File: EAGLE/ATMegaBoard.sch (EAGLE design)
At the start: 29 parts, among them IC1 L298, IC2 ATMEGA168-20P, IC3 REG1117, X1 49S/18PF

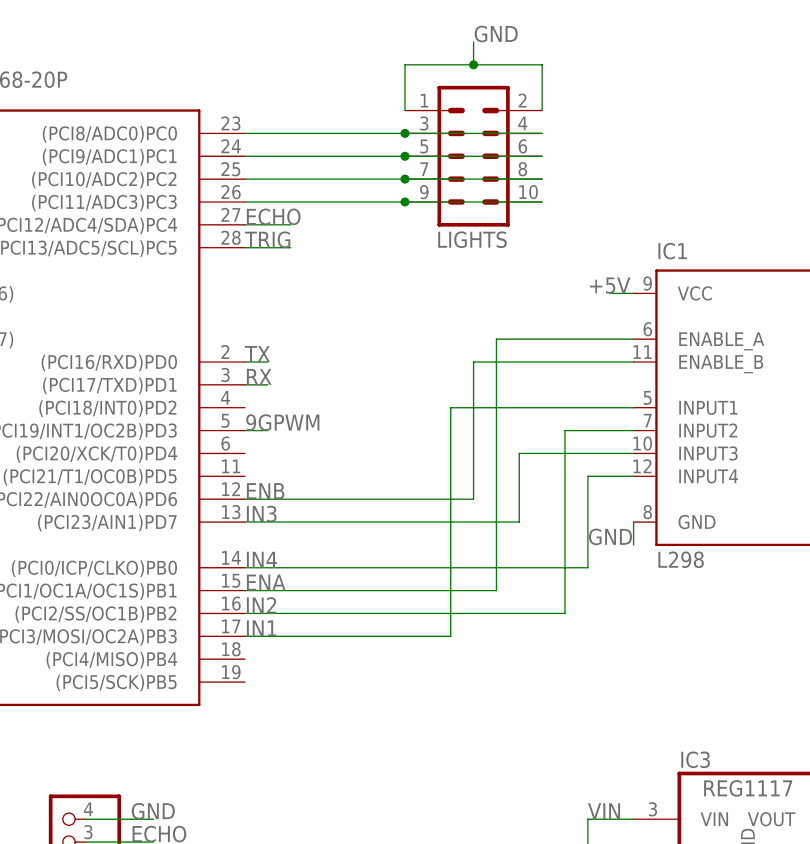
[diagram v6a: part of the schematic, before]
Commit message: updated output for LEDs
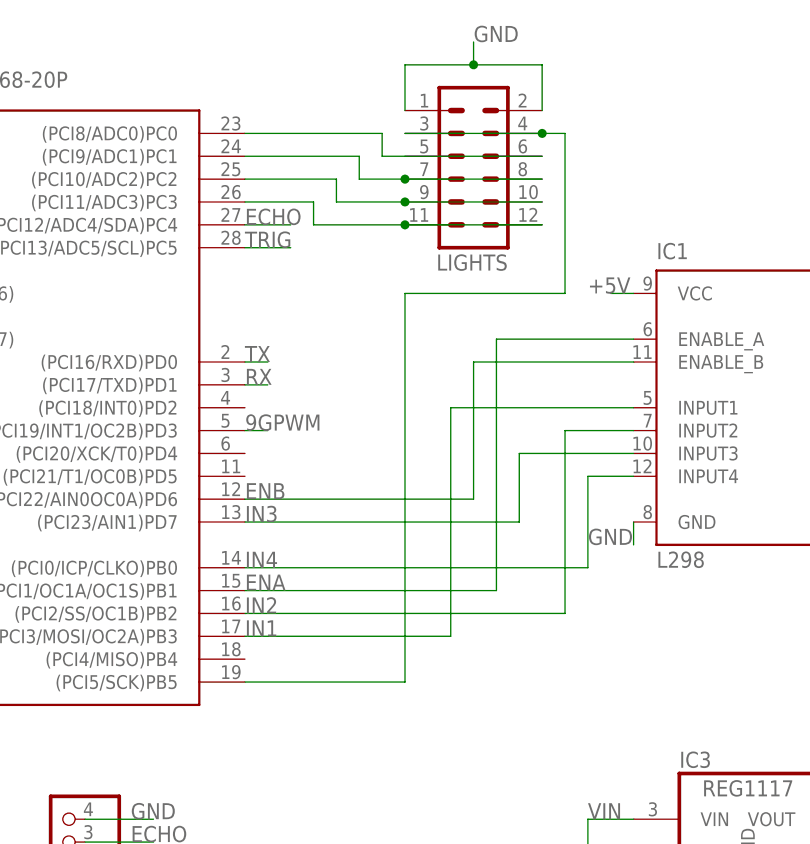
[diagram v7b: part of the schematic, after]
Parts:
- LIGHTS: device con-lstb:MA05-2 -> con-lstb:MA06-2
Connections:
- new net N$7: IC2.(PCI11/ADC3)PC3, LIGHTS.11, LIGHTS.12
- net N$1: now also IC2.(PCI5/SCK)PB5; no longer IC2.(PCI8/ADC0)PC0
- net N$2: now also IC2.(PCI8/ADC0)PC0; no longer IC2.(PCI9/ADC1)PC1
- net N$4: now also IC2.(PCI9/ADC1)PC1; no longer IC2.(PCI10/ADC2)PC2
- net N$5: now also IC2.(PCI10/ADC2)PC2; no longer IC2.(PCI11/ADC3)PC3
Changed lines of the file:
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@@
 <part name="R3" library="rcl" library_urn="urn:adsk.eagle:library:334" deviceset="R-US_" device="0207/10" package3d_urn="urn:adsk.eagle:package:23491/2" value="1k"/>
 <part name="HC05" library="con-lsta" library_urn="urn:adsk.eagle:library:161" deviceset="FE06W" device="" package3d_urn="urn:adsk.eagle:package:8198/1"/>
-<part name="LIGHTS" library="con-lstb" library_urn="urn:adsk.eagle:library:162" deviceset="MA05-2" device="" package3d_urn="urn:adsk.eagle:package:8329/1"/>
+<part name="LIGHTS" library="con-lstb" library_urn="urn:adsk.eagle:library:162" deviceset="MA06-2" device="" package3d_urn="urn:adsk.eagle:package:8342/1"/>
 </parts>
 <sheets>
@@
 <attribute name="NAME" x="110.49" y="-26.162" size="1.778" layer="95" rot="R180"/>
 </instance>
-<instance part="LIGHTS" gate="G$1" x="114.3" y="76.2" smashed="yes" rot="R180">
-<attribute name="VALUE" x="118.11" y="86.36" size="1.778" layer="96" rot="R180"/>
-<attribute name="NAME" x="118.11" y="67.818" size="1.778" layer="95" rot="R180"/>
+<instance part="LIGHTS" gate="1" x="114.3" y="73.66" smashed="yes" rot="R180">
+<attribute name="VALUE" x="118.11" y="83.82" size="1.778" layer="96" rot="R180"/>
+<attribute name="NAME" x="118.11" y="65.278" size="1.778" layer="95" rot="R180"/>
 </instance>
 </instances>
@@
 </segment>
 <segment>
-<pinref part="LIGHTS" gate="G$1" pin="1"/>
+<pinref part="LIGHTS" gate="1" pin="1"/>
 <wire x1="106.68" y1="81.28" x2="106.68" y2="86.36" width="0.1524" layer="91"/>
 <wire x1="106.68" y1="86.36" x2="114.3" y2="86.36" width="0.1524" layer="91"/>
-<pinref part="LIGHTS" gate="G$1" pin="2"/>
+<pinref part="LIGHTS" gate="1" pin="2"/>
 <wire x1="114.3" y1="86.36" x2="121.92" y2="86.36" width="0.1524" layer="91"/>
 <wire x1="121.92" y1="86.36" x2="121.92" y2="81.28" width="0.1524" layer="91"/>
@@
 <net name="N$1" class="0">
 <segment>
+<pinref part="LIGHTS" gate="1" pin="3"/>
+<pinref part="LIGHTS" gate="1" pin="4"/>
+<wire x1="106.68" y1="78.74" x2="121.92" y2="78.74" width="0.1524" layer="91"/>
+<wire x1="121.92" y1="78.74" x2="124.46" y2="78.74" width="0.1524" layer="91"/>
+<junction x="121.92" y="78.74"/>
+<wire x1="124.46" y1="78.74" x2="124.46" y2="60.96" width="0.1524" layer="91"/>
+<pinref part="IC2" gate="G$1" pin="(PCI5/SCK)PB5"/>
+<wire x1="106.68" y1="17.78" x2="88.9" y2="17.78" width="0.1524" layer="91"/>
+<wire x1="124.46" y1="60.96" x2="106.68" y2="60.96" width="0.1524" layer="91"/>
+<wire x1="106.68" y1="60.96" x2="106.68" y2="17.78" width="0.1524" layer="91"/>
+</segment>
+</net>
+<net name="N$2" class="0">
+<segment>
+<pinref part="LIGHTS" gate="1" pin="5"/>
+<pinref part="LIGHTS" gate="1" pin="6"/>
+<wire x1="106.68" y1="76.2" x2="121.92" y2="76.2" width="0.1524" layer="91"/>
 <pinref part="IC2" gate="G$1" pin="(PCI8/ADC0)PC0"/>
-<pinref part="LIGHTS" gate="G$1" pin="3"/>
-<wire x1="88.9" y1="78.74" x2="106.68" y2="78.74" width="0.1524" layer="91"/>
-<pinref part="LIGHTS" gate="G$1" pin="4"/>
-<wire x1="106.68" y1="78.74" x2="121.92" y2="78.74" width="0.1524" layer="91"/>
-<junction x="106.68" y="78.74"/>
-</segment>
-</net>
-<net name="N$2" class="0">
-<segment>
+<wire x1="88.9" y1="78.74" x2="104.14" y2="78.74" width="0.1524" layer="91"/>
+<wire x1="104.14" y1="78.74" x2="104.14" y2="76.2" width="0.1524" layer="91"/>
+<wire x1="104.14" y1="76.2" x2="106.68" y2="76.2" width="0.1524" layer="91"/>
+</segment>
+</net>
+<net name="N$4" class="0">
+<segment>
+<pinref part="LIGHTS" gate="1" pin="7"/>
+<pinref part="LIGHTS" gate="1" pin="8"/>
+<wire x1="106.68" y1="73.66" x2="121.92" y2="73.66" width="0.1524" layer="91"/>
 <pinref part="IC2" gate="G$1" pin="(PCI9/ADC1)PC1"/>
-<pinref part="LIGHTS" gate="G$1" pin="5"/>
-<wire x1="88.9" y1="76.2" x2="106.68" y2="76.2" width="0.1524" layer="91"/>
-<pinref part="LIGHTS" gate="G$1" pin="6"/>
-<wire x1="106.68" y1="76.2" x2="121.92" y2="76.2" width="0.1524" layer="91"/>
-<junction x="106.68" y="76.2"/>
-</segment>
-</net>
-<net name="N$4" class="0">
-<segment>
+<wire x1="88.9" y1="76.2" x2="101.6" y2="76.2" width="0.1524" layer="91"/>
+<wire x1="101.6" y1="76.2" x2="101.6" y2="73.66" width="0.1524" layer="91"/>
+<wire x1="101.6" y1="73.66" x2="106.68" y2="73.66" width="0.1524" layer="91"/>
+<junction x="106.68" y="73.66"/>
+</segment>
+</net>
+<net name="N$5" class="0">
+<segment>
+<pinref part="LIGHTS" gate="1" pin="9"/>
+<pinref part="LIGHTS" gate="1" pin="10"/>
+<wire x1="106.68" y1="71.12" x2="121.92" y2="71.12" width="0.1524" layer="91"/>
 <pinref part="IC2" gate="G$1" pin="(PCI10/ADC2)PC2"/>
-<pinref part="LIGHTS" gate="G$1" pin="7"/>
-<wire x1="88.9" y1="73.66" x2="106.68" y2="73.66" width="0.1524" layer="91"/>
-<pinref part="LIGHTS" gate="G$1" pin="8"/>
-<wire x1="106.68" y1="73.66" x2="121.92" y2="73.66" width="0.1524" layer="91"/>
-<junction x="106.68" y="73.66"/>
-</segment>
-</net>
-<net name="N$5" class="0">
-<segment>
+<wire x1="88.9" y1="73.66" x2="99.06" y2="73.66" width="0.1524" layer="91"/>
+<wire x1="99.06" y1="73.66" x2="99.06" y2="71.12" width="0.1524" layer="91"/>
+<wire x1="99.06" y1="71.12" x2="106.68" y2="71.12" width="0.1524" layer="91"/>
+<junction x="106.68" y="71.12"/>
+</segment>
+</net>
+<net name="N$7" class="0">
+<segment>
+<pinref part="LIGHTS" gate="1" pin="12"/>
+<pinref part="LIGHTS" gate="1" pin="11"/>
+<wire x1="106.68" y1="68.58" x2="121.92" y2="68.58" width="0.1524" layer="91"/>
 <pinref part="IC2" gate="G$1" pin="(PCI11/ADC3)PC3"/>
-<pinref part="LIGHTS" gate="G$1" pin="9"/>
-<wire x1="88.9" y1="71.12" x2="106.68" y2="71.12" width="0.1524" layer="91"/>
-<pinref part="LIGHTS" gate="G$1" pin="10"/>
-<wire x1="106.68" y1="71.12" x2="121.92" y2="71.12" width="0.1524" layer="91"/>
-<junction x="106.68" y="71.12"/>
-</segment>
-</net>
+<wire x1="88.9" y1="71.12" x2="96.52" y2="71.12" width="0.1524" layer="91"/>
+<wire x1="96.52" y1="71.12" x2="96.52" y2="68.58" width="0.1524" layer="91"/>
+<wire x1="96.52" y1="68.58" x2="106.68" y2="68.58" width="0.1524" layer="91"/>
+<junction x="106.68" y="68.58"/>
+</segment>
+</net>

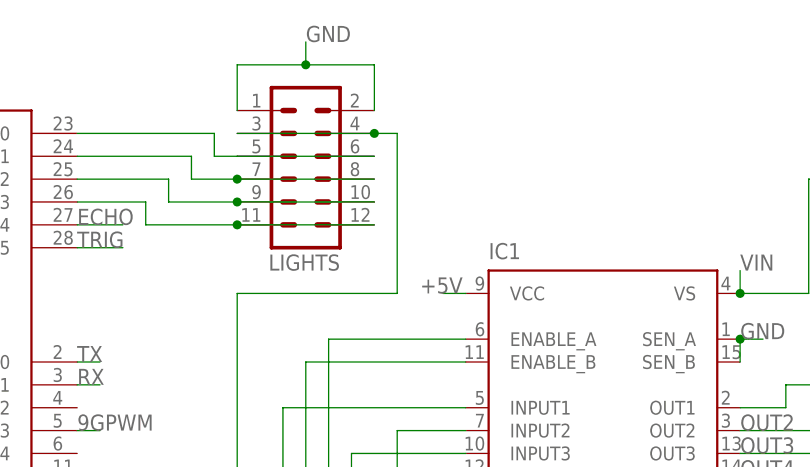
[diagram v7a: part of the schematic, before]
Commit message: expanded LED lighting to be 1 to 1
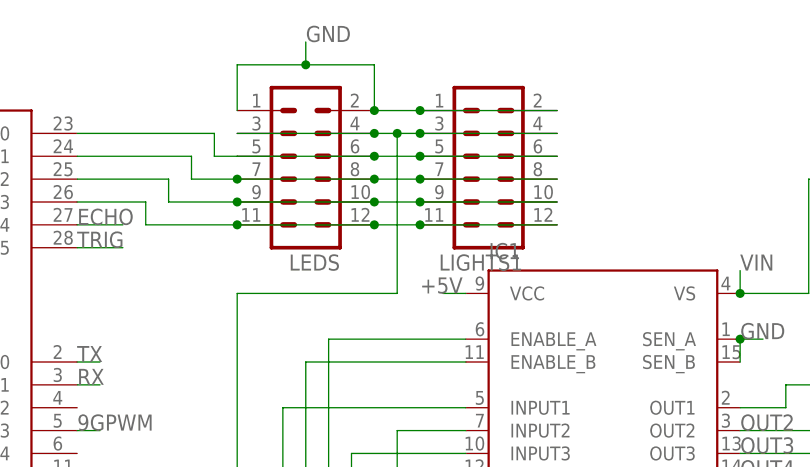
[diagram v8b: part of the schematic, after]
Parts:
- added LIGHTS1: (no value), con-lstb:MA06-2
- renumbered LIGHTS to LEDS
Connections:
- removed net N$1: IC2.(PCI5/SCK)PB5, LEDS.3, LEDS.4
- new net N$6: IC2.(PCI5/SCK)PB5, LEDS.3, LEDS.4, LIGHTS1.3, LIGHTS1.4
- net GND: now also LIGHTS1.1, LIGHTS1.2
- net N$2: now also LIGHTS1.5, LIGHTS1.6
- net N$4: now also LIGHTS1.7, LIGHTS1.8
- net N$5: now also LIGHTS1.10, LIGHTS1.9
- net N$7: now also LIGHTS1.11, LIGHTS1.12
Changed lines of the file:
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@@
 <part name="R3" library="rcl" library_urn="urn:adsk.eagle:library:334" deviceset="R-US_" device="0207/10" package3d_urn="urn:adsk.eagle:package:23491/2" value="1k"/>
 <part name="HC05" library="con-lsta" library_urn="urn:adsk.eagle:library:161" deviceset="FE06W" device="" package3d_urn="urn:adsk.eagle:package:8198/1"/>
-<part name="LIGHTS" library="con-lstb" library_urn="urn:adsk.eagle:library:162" deviceset="MA06-2" device="" package3d_urn="urn:adsk.eagle:package:8342/1"/>
+<part name="LEDS" library="con-lstb" library_urn="urn:adsk.eagle:library:162" deviceset="MA06-2" device="" package3d_urn="urn:adsk.eagle:package:8342/1"/>
+<part name="LIGHTS1" library="con-lstb" library_urn="urn:adsk.eagle:library:162" deviceset="MA06-2" device="" package3d_urn="urn:adsk.eagle:package:8342/1"/>
 </parts>
 <sheets>
@@
 <attribute name="NAME" x="110.49" y="-26.162" size="1.778" layer="95" rot="R180"/>
 </instance>
-<instance part="LIGHTS" gate="1" x="114.3" y="73.66" smashed="yes" rot="R180">
+<instance part="LEDS" gate="1" x="114.3" y="73.66" smashed="yes" rot="R180">
 <attribute name="VALUE" x="118.11" y="83.82" size="1.778" layer="96" rot="R180"/>
 <attribute name="NAME" x="118.11" y="65.278" size="1.778" layer="95" rot="R180"/>
+</instance>
+<instance part="LIGHTS1" gate="1" x="134.62" y="73.66" smashed="yes" rot="R180">
+<attribute name="VALUE" x="138.43" y="83.82" size="1.778" layer="96" rot="R180"/>
+<attribute name="NAME" x="138.43" y="65.278" size="1.778" layer="95" rot="R180"/>
 </instance>
 </instances>
@@
 </segment>
 <segment>
-<pinref part="LIGHTS" gate="1" pin="1"/>
+<pinref part="LEDS" gate="1" pin="1"/>
 <wire x1="106.68" y1="81.28" x2="106.68" y2="86.36" width="0.1524" layer="91"/>
 <wire x1="106.68" y1="86.36" x2="114.3" y2="86.36" width="0.1524" layer="91"/>
-<pinref part="LIGHTS" gate="1" pin="2"/>
+<pinref part="LEDS" gate="1" pin="2"/>
 <wire x1="114.3" y1="86.36" x2="121.92" y2="86.36" width="0.1524" layer="91"/>
 <wire x1="121.92" y1="86.36" x2="121.92" y2="81.28" width="0.1524" layer="91"/>
@@
 <junction x="114.3" y="86.36"/>
 <label x="114.3" y="88.9" size="1.778" layer="95"/>
+<pinref part="LIGHTS1" gate="1" pin="1"/>
+<wire x1="121.92" y1="81.28" x2="127" y2="81.28" width="0.1524" layer="91"/>
+<junction x="121.92" y="81.28"/>
+<pinref part="LIGHTS1" gate="1" pin="2"/>
+<wire x1="127" y1="81.28" x2="142.24" y2="81.28" width="0.1524" layer="91"/>
+<junction x="127" y="81.28"/>
 </segment>
 </net>
@@
 </segment>
 </net>
-<net name="N$1" class="0">
-<segment>
-<pinref part="LIGHTS" gate="1" pin="3"/>
-<pinref part="LIGHTS" gate="1" pin="4"/>
+<net name="N$4" class="0">
+<segment>
+<pinref part="LEDS" gate="1" pin="7"/>
+<pinref part="LEDS" gate="1" pin="8"/>
+<wire x1="106.68" y1="73.66" x2="121.92" y2="73.66" width="0.1524" layer="91"/>
+<pinref part="IC2" gate="G$1" pin="(PCI9/ADC1)PC1"/>
+<wire x1="88.9" y1="76.2" x2="101.6" y2="76.2" width="0.1524" layer="91"/>
+<wire x1="101.6" y1="76.2" x2="101.6" y2="73.66" width="0.1524" layer="91"/>
+<wire x1="101.6" y1="73.66" x2="106.68" y2="73.66" width="0.1524" layer="91"/>
+<junction x="106.68" y="73.66"/>
+<pinref part="LIGHTS1" gate="1" pin="7"/>
+<wire x1="121.92" y1="73.66" x2="127" y2="73.66" width="0.1524" layer="91"/>
+<junction x="121.92" y="73.66"/>
+<pinref part="LIGHTS1" gate="1" pin="8"/>
+<wire x1="127" y1="73.66" x2="142.24" y2="73.66" width="0.1524" layer="91"/>
+<junction x="127" y="73.66"/>
+</segment>
+</net>
+<net name="N$7" class="0">
+<segment>
+<pinref part="LEDS" gate="1" pin="12"/>
+<pinref part="LEDS" gate="1" pin="11"/>
+<wire x1="106.68" y1="68.58" x2="121.92" y2="68.58" width="0.1524" layer="91"/>
+<pinref part="IC2" gate="G$1" pin="(PCI11/ADC3)PC3"/>
+<wire x1="88.9" y1="71.12" x2="96.52" y2="71.12" width="0.1524" layer="91"/>
+<wire x1="96.52" y1="71.12" x2="96.52" y2="68.58" width="0.1524" layer="91"/>
+<wire x1="96.52" y1="68.58" x2="106.68" y2="68.58" width="0.1524" layer="91"/>
+<junction x="106.68" y="68.58"/>
+<pinref part="LIGHTS1" gate="1" pin="11"/>
+<wire x1="121.92" y1="68.58" x2="127" y2="68.58" width="0.1524" layer="91"/>
+<junction x="121.92" y="68.58"/>
+<pinref part="LIGHTS1" gate="1" pin="12"/>
+<wire x1="127" y1="68.58" x2="142.24" y2="68.58" width="0.1524" layer="91"/>
+<junction x="127" y="68.58"/>
+</segment>
+</net>
+<net name="N$6" class="0">
+<segment>
+<pinref part="LIGHTS1" gate="1" pin="3"/>
+<pinref part="LIGHTS1" gate="1" pin="4"/>
+<wire x1="127" y1="78.74" x2="142.24" y2="78.74" width="0.1524" layer="91"/>
+<pinref part="LEDS" gate="1" pin="3"/>
+<pinref part="LEDS" gate="1" pin="4"/>
 <wire x1="106.68" y1="78.74" x2="121.92" y2="78.74" width="0.1524" layer="91"/>
 <wire x1="121.92" y1="78.74" x2="124.46" y2="78.74" width="0.1524" layer="91"/>
@@
 <wire x1="124.46" y1="60.96" x2="106.68" y2="60.96" width="0.1524" layer="91"/>
 <wire x1="106.68" y1="60.96" x2="106.68" y2="17.78" width="0.1524" layer="91"/>
+<wire x1="127" y1="78.74" x2="124.46" y2="78.74" width="0.1524" layer="91"/>
+<junction x="127" y="78.74"/>
+<junction x="124.46" y="78.74"/>
 </segment>
 </net>
 <net name="N$2" class="0">
 <segment>
-<pinref part="LIGHTS" gate="1" pin="5"/>
-<pinref part="LIGHTS" gate="1" pin="6"/>
+<pinref part="LIGHTS1" gate="1" pin="5"/>
+<pinref part="LIGHTS1" gate="1" pin="6"/>
+<wire x1="127" y1="76.2" x2="142.24" y2="76.2" width="0.1524" layer="91"/>
+<pinref part="LEDS" gate="1" pin="5"/>
+<pinref part="LEDS" gate="1" pin="6"/>
 <wire x1="106.68" y1="76.2" x2="121.92" y2="76.2" width="0.1524" layer="91"/>
 <pinref part="IC2" gate="G$1" pin="(PCI8/ADC0)PC0"/>
@@
 <wire x1="104.14" y1="78.74" x2="104.14" y2="76.2" width="0.1524" layer="91"/>
 <wire x1="104.14" y1="76.2" x2="106.68" y2="76.2" width="0.1524" layer="91"/>
-</segment>
-</net>
-<net name="N$4" class="0">
-<segment>
-<pinref part="LIGHTS" gate="1" pin="7"/>
-<pinref part="LIGHTS" gate="1" pin="8"/>
-<wire x1="106.68" y1="73.66" x2="121.92" y2="73.66" width="0.1524" layer="91"/>
-<pinref part="IC2" gate="G$1" pin="(PCI9/ADC1)PC1"/>
-<wire x1="88.9" y1="76.2" x2="101.6" y2="76.2" width="0.1524" layer="91"/>
-<wire x1="101.6" y1="76.2" x2="101.6" y2="73.66" width="0.1524" layer="91"/>
-<wire x1="101.6" y1="73.66" x2="106.68" y2="73.66" width="0.1524" layer="91"/>
-<junction x="106.68" y="73.66"/>
+<wire x1="127" y1="76.2" x2="121.92" y2="76.2" width="0.1524" layer="91"/>
+<junction x="127" y="76.2"/>
+<junction x="121.92" y="76.2"/>
 </segment>
 </net>
 <net name="N$5" class="0">
 <segment>
-<pinref part="LIGHTS" gate="1" pin="9"/>
-<pinref part="LIGHTS" gate="1" pin="10"/>
+<pinref part="LIGHTS1" gate="1" pin="10"/>
+<pinref part="LIGHTS1" gate="1" pin="9"/>
+<wire x1="142.24" y1="71.12" x2="127" y2="71.12" width="0.1524" layer="91"/>
+<pinref part="LEDS" gate="1" pin="9"/>
+<pinref part="LEDS" gate="1" pin="10"/>
 <wire x1="106.68" y1="71.12" x2="121.92" y2="71.12" width="0.1524" layer="91"/>
 <pinref part="IC2" gate="G$1" pin="(PCI10/ADC2)PC2"/>
@@
 <wire x1="99.06" y1="71.12" x2="106.68" y2="71.12" width="0.1524" layer="91"/>
 <junction x="106.68" y="71.12"/>
-</segment>
-</net>
-<net name="N$7" class="0">
-<segment>
-<pinref part="LIGHTS" gate="1" pin="12"/>
-<pinref part="LIGHTS" gate="1" pin="11"/>
-<wire x1="106.68" y1="68.58" x2="121.92" y2="68.58" width="0.1524" layer="91"/>
-<pinref part="IC2" gate="G$1" pin="(PCI11/ADC3)PC3"/>
-<wire x1="88.9" y1="71.12" x2="96.52" y2="71.12" width="0.1524" layer="91"/>
-<wire x1="96.52" y1="71.12" x2="96.52" y2="68.58" width="0.1524" layer="91"/>
-<wire x1="96.52" y1="68.58" x2="106.68" y2="68.58" width="0.1524" layer="91"/>
-<junction x="106.68" y="68.58"/>
-</segment>
-</net>
+<wire x1="127" y1="71.12" x2="121.92" y2="71.12" width="0.1524" layer="91"/>
+<junction x="127" y="71.12"/>
+<junction x="121.92" y="71.12"/>
+</segment>
+</net>
